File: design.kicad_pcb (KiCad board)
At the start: 2 copper layers, 35.1 x 15 mm, 20 parts, among them J1 USB_C_Receptacle, J2 Conn_01x05, Q1 2N7002K, Q2 2N7002K, Q3 2N7002K, U1 ATtiny814-SS

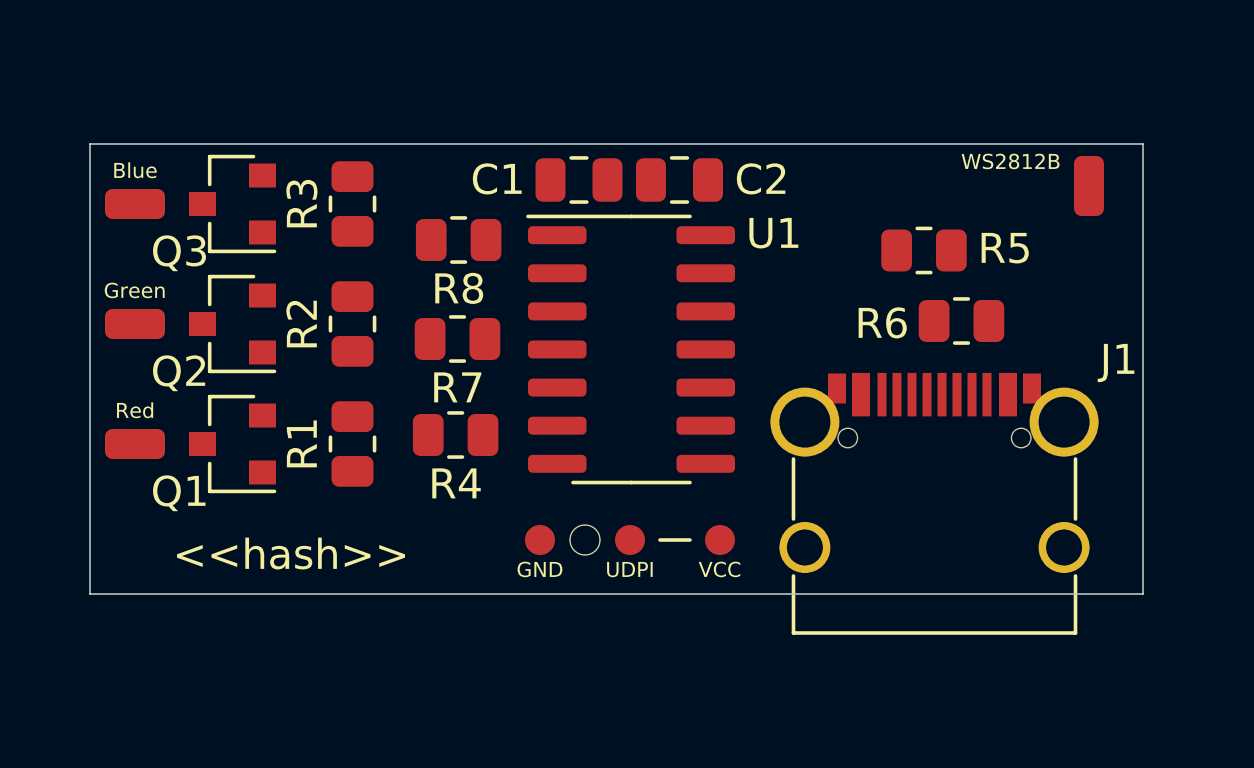
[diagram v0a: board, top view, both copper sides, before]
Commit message: PCB: add 5V, rotate USB-C
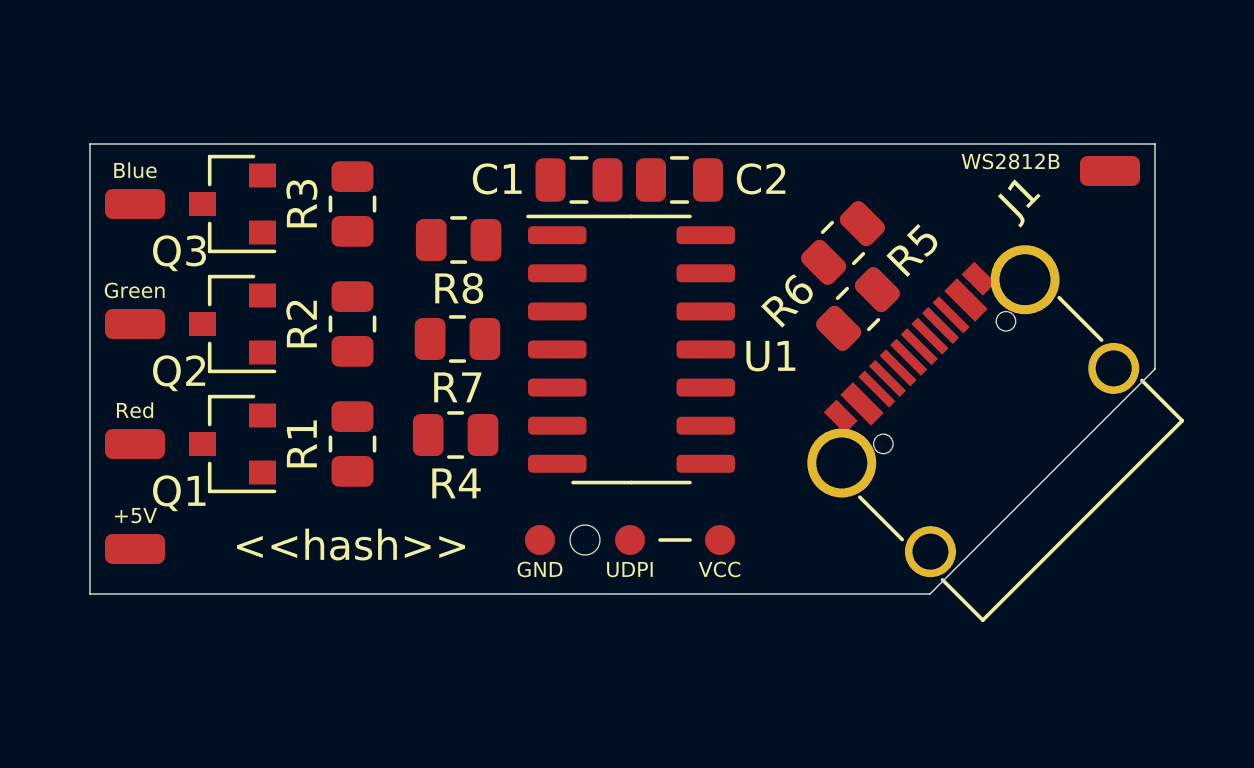
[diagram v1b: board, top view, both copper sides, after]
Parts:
- added TP5: TestPoint, Connector_Wire:SolderWirePad_1x01_SMD_1x2mm, F.Cu at (138.0, 93.5)
- moved R6 4.73 mm to (161.6, 83.3), turned to 225 degrees
- moved J1 3.40 mm to (166.8, 89.8), turned to 45 degrees
- moved R5 2.94 mm to (162.1, 85.5), turned to 45 degrees
- moved TP4 0.86 mm to (170.5, 80.9), turned to 90 degrees
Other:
- board size 35.1 x 15 mm -> 35.5 x 15 mm
- board text added: "+5V"

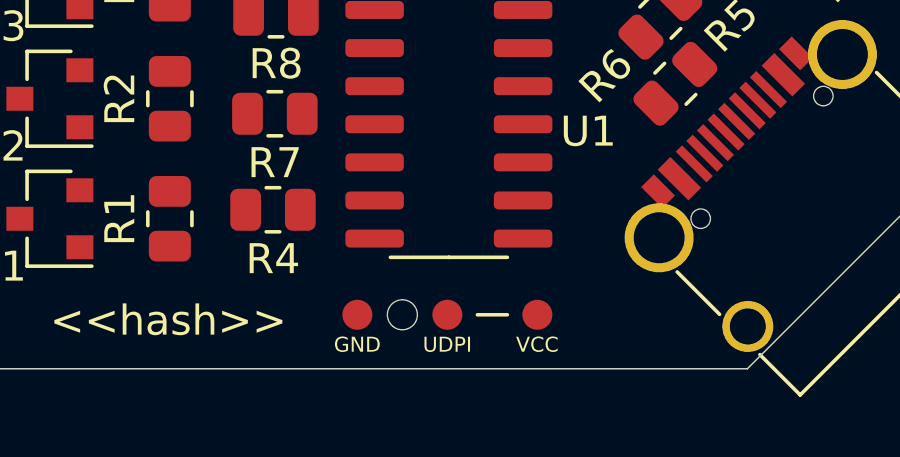
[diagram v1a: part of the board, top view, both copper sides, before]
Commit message: PCB: update udpi footprint
GND in middle
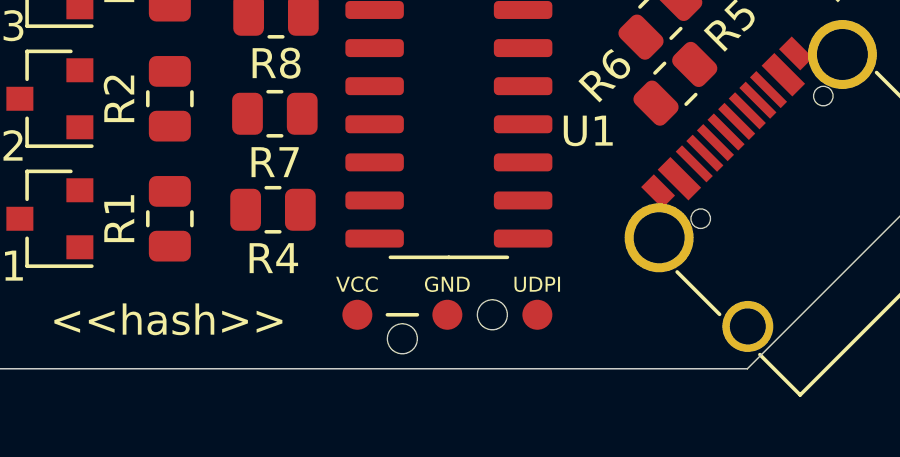
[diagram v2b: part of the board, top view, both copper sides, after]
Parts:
- turned J2 to 0 degrees
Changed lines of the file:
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@@
     (add_net WS2812b)
+  )
+  (module E32-xxxT20D:UDPI_interface_small (layer F.Cu)
+    (at 154.5 93.2)
+    (fp_text reference J2 (at 0 -2.5) (layer F.SilkS) hide
+      (effects (font (size 1 1) (thickness 0.15)))
+    )
+    (fp_text value Conn_01x05 (at 0 -4) (layer F.Fab)
+      (effects (font (size 1 1) (thickness 0.15)))
+    )
+    (fp_text user VCC (at -3 -1) (layer F.SilkS)
+      (effects (font (size 0.5 0.5) (thickness 0.125)))
+    )
+    (fp_text user UDPI (at 3 -1) (layer F.SilkS)
+      (effects (font (size 0.5 0.5) (thickness 0.125)))
+    )
+    (fp_text user GND (at 0 -1) (layer F.SilkS)
+      (effects (font (size 0.5 0.5) (thickness 0.125)))
+    )
+    (fp_line (start -2 0) (end -1 0) (layer F.SilkS) (width 0.12))
+    (pad "" np_thru_hole circle (at -1.5 0.8) (size 1 1) (drill 1) (layers *.Cu *.Mask))
+    (pad "" np_thru_hole circle (at 1.5 0) (size 1 1) (drill 1) (layers *.Cu *.Mask))
+    (pad 1 smd circle (at 3 0) (size 1 1) (layers F.Cu F.Paste F.Mask)
+      (net 25 UDPI))
+    (pad 2 smd circle (at -3 0) (size 1 1) (layers F.Cu F.Paste F.Mask)
+      (net 22 VCC))
+    (pad 3 smd circle (at 0 0) (size 1 1) (layers F.Cu F.Paste F.Mask)
+      (net 15 GND))
   )
   (module Connector_Wire:SolderWirePad_1x01_SMD_1x2mm (layer F.Cu)
@@
     )
   )
-  (module E32-xxxT20D:UDPI_interface_small (layer F.Cu)
-    (at 154.5 93.2 180)
-    (fp_text reference J2 (at 0 -2.5) (layer F.SilkS) hide
-      (effects (font (size 1 1) (thickness 0.15)))
-    )
-    (fp_text value Conn_01x05 (at 0 -4) (layer F.Fab)
-      (effects (font (size 1 1) (thickness 0.15)))
-    )
-    (fp_line (start -2 0) (end -1 0) (layer F.SilkS) (width 0.12))
-    (fp_text user VCC (at -3 -1) (layer F.SilkS)
-      (effects (font (size 0.5 0.5) (thickness 0.125)))
-    )
-    (fp_text user GND (at 3 -1) (layer F.SilkS)
-      (effects (font (size 0.5 0.5) (thickness 0.125)))
-    )
-    (fp_text user UDPI (at 0 -1) (layer F.SilkS)
-      (effects (font (size 0.5 0.5) (thickness 0.125)))
-    )
-    (pad "" np_thru_hole circle (at 1.5 0 180) (size 1 1) (drill 1) (layers *.Cu *.Mask))
-    (pad 3 smd circle (at 3 0 180) (size 1 1) (layers F.Cu F.Paste F.Mask)
-      (net 15 GND))
-    (pad 2 smd circle (at -3 0 180) (size 1 1) (layers F.Cu F.Paste F.Mask)
-      (net 22 VCC))
-    (pad 1 smd circle (at 0 0 180) (size 1 1) (layers F.Cu F.Paste F.Mask)
-      (net 25 UDPI))
-  )
   (module Connector_USB:USB_C_Receptacle_HRO_TYPE-C-31-M-12_simple (layer F.Cu)

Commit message: PCB: routing
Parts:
- moved J2 17.6 mm to (167.7, 81.6), turned to 180 degrees
- moved TP4 11.1 mm to (159.4, 81.3), turned to 180 degrees
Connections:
- TP5 pad 1: +5V -> VCC
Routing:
- net VCC: track 0.00 -> 15.5 mm
- net UDPI: track 0.00 -> 12.8 mm
- net GND: track 0.00 -> 8.28 mm, vias 0 -> 5
- net Net-(Q1-Pad1): track 0.00 -> 6.04 mm
- net Net-(Q2-Pad1): track 0.00 -> 5.77 mm
- net Net-(Q3-Pad1): track 0.00 -> 5.76 mm
- net WS2812b: track 0.00 -> 4.56 mm
- net Net-(J1-PadB5): track 0.00 -> 4.27 mm
- net Blue_PWM: track 0.00 -> 2.83 mm
- net Green_PWM: track 0.00 -> 2.79 mm
- net Red_PWM: track 0.00 -> 2.60 mm
- net Net-(J1-PadA5): track 0.00 -> 2.34 mm
- net Red_neg: track 0.00 -> 2.25 mm
- net Green_neg: track 0.00 -> 2.25 mm
- net Blue_neg: track 0.00 -> 2.25 mm
- added copper zone on B.Cu, net GND
- added copper zone on F.Cu, net GND
- added copper zone on F.Cu, net VCC
